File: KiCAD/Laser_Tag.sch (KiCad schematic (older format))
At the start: 20 parts, among them M1 MICROPHONE, P1 PHOTODETECTOR, Q1 2N3904, SW1 SW_PUSH, U1 PIC12LF

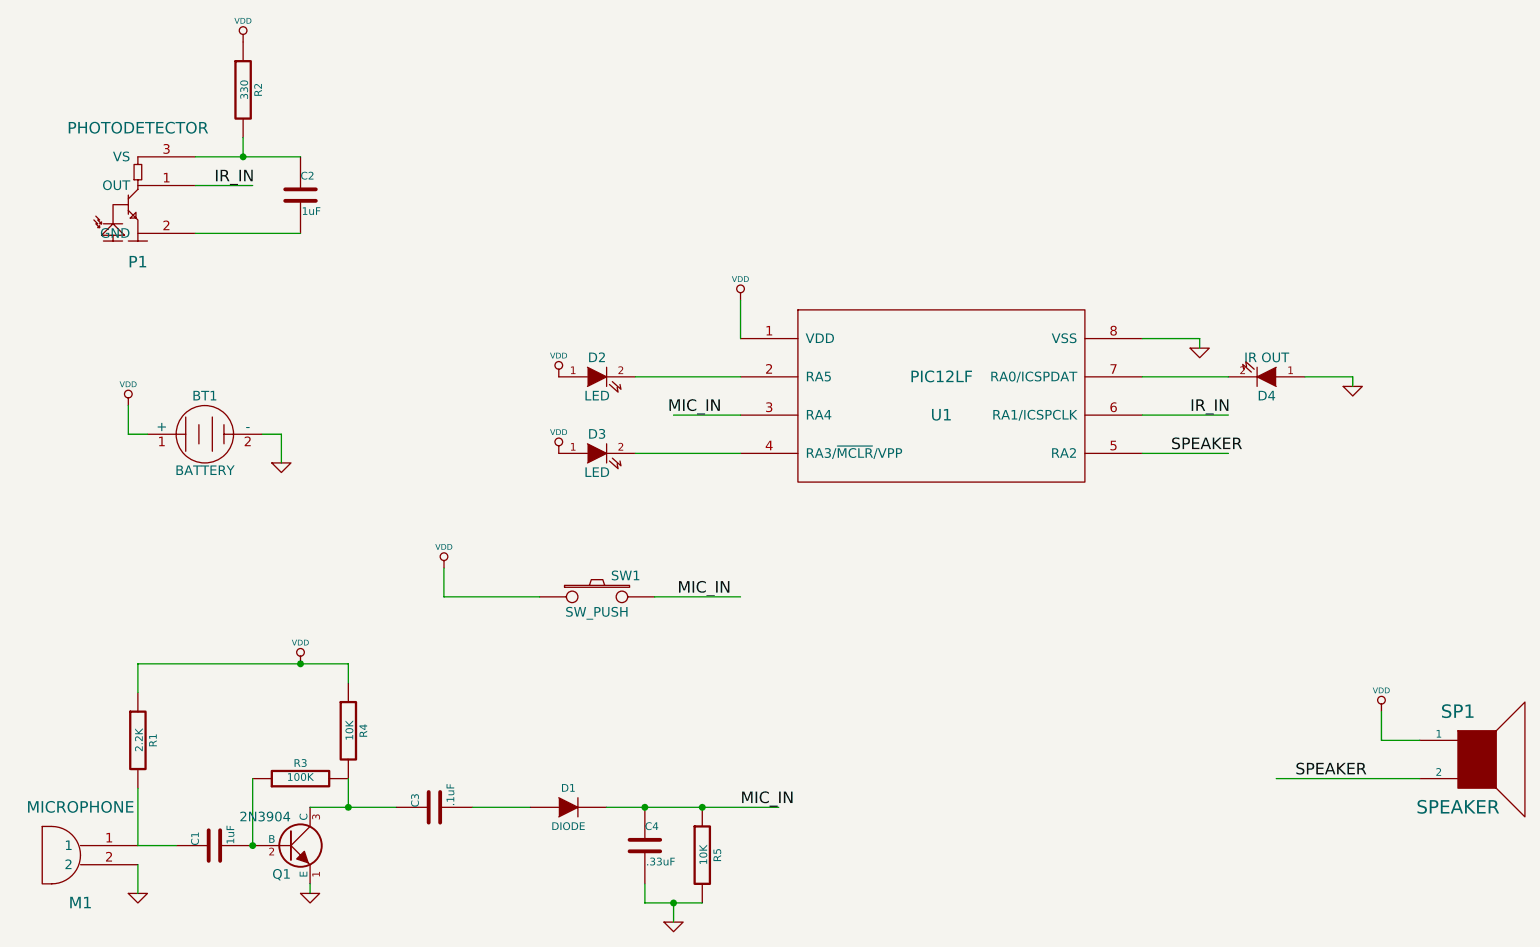
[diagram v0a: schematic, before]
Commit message: Changed component values, added video
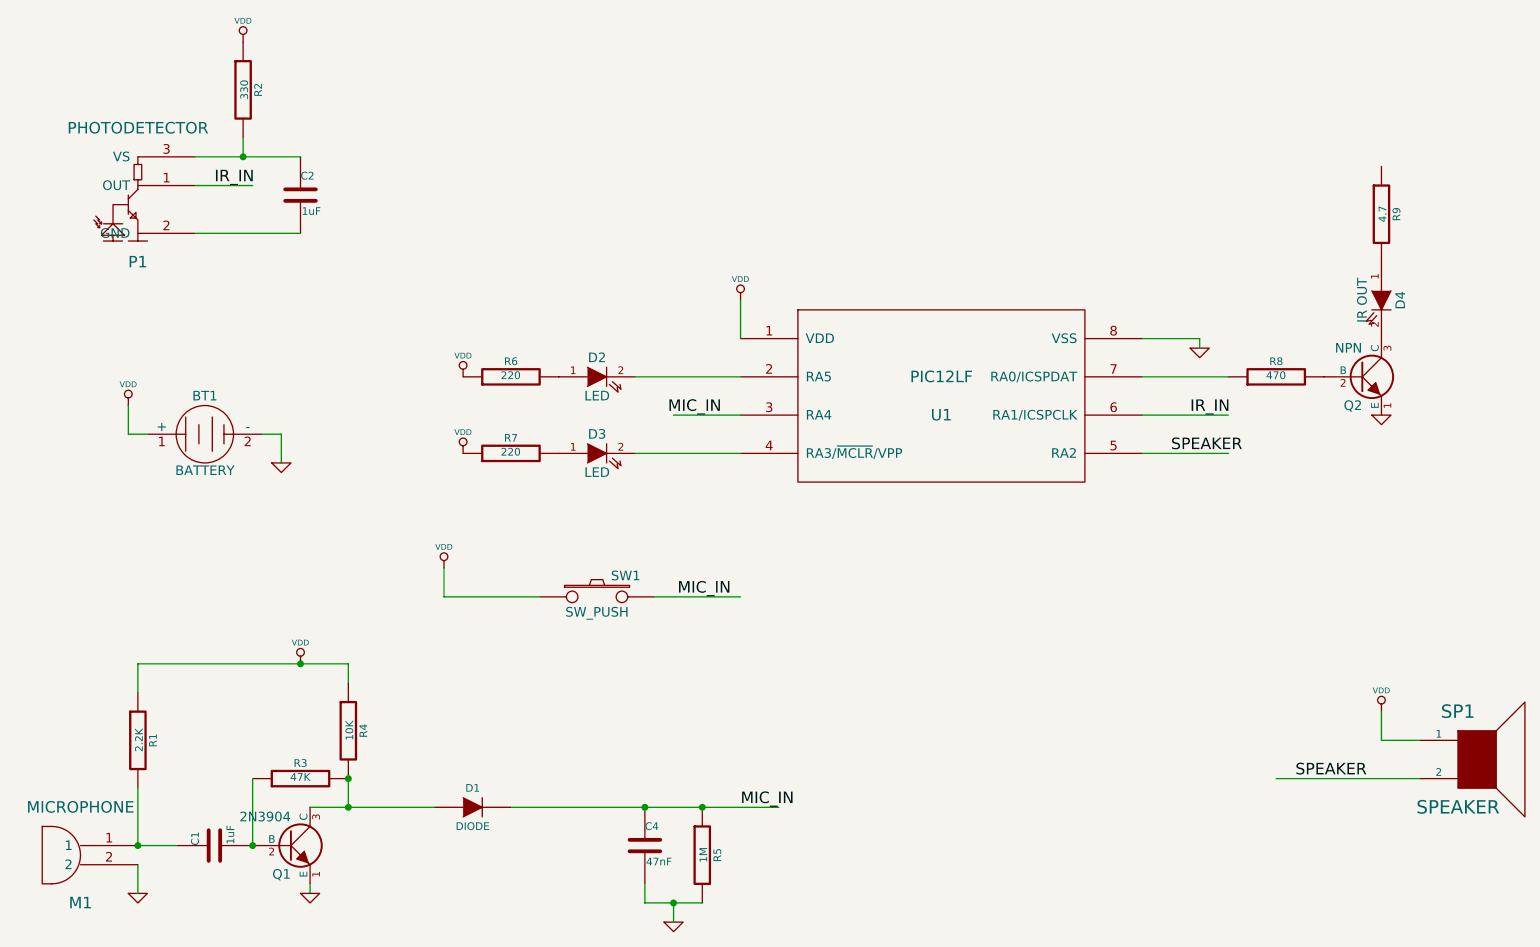
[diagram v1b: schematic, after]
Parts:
- removed C3: .1uF, ~, symbol C
- added Q2: NPN, ~, symbol NPN
- added R6, R7: 220, ~, symbol R
- added R8: 470, ~, symbol R
- added R9: 4.7, ~, symbol R
- C4: value .33uF -> 47nF
- R3: value 100K -> 47K
- R5: value 10K -> 1M
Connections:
- wire segments 40 -> 37
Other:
- moved on the sheet: D1, D4
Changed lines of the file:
@@
 Sheet 1 1
 Title ""
-Date "27 jul 2014"
+Date "28 jul 2014"
 Rev ""
 Comp ""
@@
 P 3850 5600
 F 0 "R3" V 3930 5600 40  0000 C CNN
-F 1 "100K" V 3857 5601 40  0000 C CNN
+F 1 "47K" V 3857 5601 40  0000 C CNN
 F 2 "~" V 3780 5600 30  0000 C CNN
 F 3 "~" H 3850 5600 30  0000 C CNN
@@
 	1    0    0    -1
 $EndComp
-$Comp
-L C C3
-U 1 1 53D53243
-P 4550 5750
-F 0 "C3" H 4550 5850 40  0000 L CNN
-F 1 ".1uF" H 4556 5665 40  0000 L CNN
-F 2 "~" H 4588 5600 30  0000 C CNN
-F 3 "~" H 4550 5750 60  0000 C CNN
-	1    4550 5750
-	0    -1   -1   0
-$EndComp
 Text Label 6150 5750 0    60   ~ 0
 MIC_IN
@@
 L LED D4
 U 1 1 53D53960
-P 8900 3500
-F 0 "D4" H 8900 3600 50  0000 C CNN
-F 1 "IR OUT" H 8900 3400 50  0000 C CNN
-F 2 "~" H 8900 3500 60  0000 C CNN
-F 3 "~" H 8900 3500 60  0000 C CNN
-	1    8900 3500
-	-1   0    0    1
+P 9500 3100
+F 0 "D4" H 9500 3200 50  0000 C CNN
+F 1 "IR OUT" H 9500 3000 50  0000 C CNN
+F 2 "~" H 9500 3100 60  0000 C CNN
+F 3 "~" H 9500 3100 60  0000 C CNN
+	1    9500 3100
+	0    1    1    0
 $EndComp
 Text Label 9050 5600 0    60   ~ 0
 SPEAKER
-Wire Wire Line
-	6150 3100 6150 3300
-Wire Wire Line
-	8250 3300 8550 3300
-Wire Wire Line
-	8550 3300 8550 3350
-Wire Wire Line
-	8950 5600 9700 5600
-Wire Wire Line
-	6150 3700 5800 3700
-Wire Wire Line
-	3000 5650 3000 5950
-Wire Wire Line
-	3000 6050 3000 6200
-Wire Wire Line
-	3000 5950 3200 5950
-Wire Wire Line
-	3900 6150 3900 6200
-Wire Wire Line
-	3000 5000 4100 5000
-Wire Wire Line
-	4100 5000 4100 5100
-Wire Wire Line
-	3000 5150 3000 5000
-Connection ~ 3850 5000
-Wire Wire Line
-	3600 5600 3600 5950
-Wire Wire Line
-	3900 5750 4350 5750
-Wire Wire Line
-	4100 5750 4100 5600
-Connection ~ 3600 5950
-Connection ~ 4100 5750
-Wire Wire Line
-	4750 5750 5050 5750
-Wire Wire Line
-	3300 2350 3850 2350
-Wire Wire Line
-	3550 2350 3550 2250
-Connection ~ 3550 2350
-Wire Wire Line
-	3300 2750 3850 2750
-Wire Wire Line
-	3300 2500 3600 2500
-Wire Wire Line
-	8250 3500 8700 3500
-Wire Wire Line
-	8250 3700 8700 3700
 Text Label 8500 3700 0    60   ~ 0
 IR_IN
-Wire Wire Line
-	8250 3900 8700 3900
 Text Label 8400 3900 0    60   ~ 0
 SPEAKER
@@
 	1    0    0    -1
 $EndComp
-Wire Wire Line
-	9500 5250 9500 5400
-Wire Wire Line
-	9500 5400 9700 5400
 $Comp
 L LED D2
@@
 L VDD #PWR8
 U 1 1 53D53E42
-P 5200 3500
-F 0 "#PWR8" H 5200 3600 30  0001 C CNN
-F 1 "VDD" H 5200 3610 30  0000 C CNN
-F 2 "" H 5200 3500 60  0000 C CNN
-F 3 "" H 5200 3500 60  0000 C CNN
-	1    5200 3500
+P 4700 3500
+F 0 "#PWR8" H 4700 3600 30  0001 C CNN
+F 1 "VDD" H 4700 3610 30  0000 C CNN
+F 2 "" H 4700 3500 60  0000 C CNN
+F 3 "" H 4700 3500 60  0000 C CNN
+	1    4700 3500
 	1    0    0    -1
 $EndComp
@@
 L VDD #PWR9
 U 1 1 53D53E51
-P 5200 3900
-F 0 "#PWR9" H 5200 4000 30  0001 C CNN
-F 1 "VDD" H 5200 4010 30  0000 C CNN
-F 2 "" H 5200 3900 60  0000 C CNN
-F 3 "" H 5200 3900 60  0000 C CNN
-	1    5200 3900
-	1    0    0    -1
-$EndComp
-Wire Wire Line
-	5600 3500 6150 3500
-Wire Wire Line
-	5600 3900 6150 3900
+P 4700 3900
+F 0 "#PWR9" H 4700 4000 30  0001 C CNN
+F 1 "VDD" H 4700 4010 30  0000 C CNN
+F 2 "" H 4700 3900 60  0000 C CNN
+F 3 "" H 4700 3900 60  0000 C CNN
+	1    4700 3900
+	1    0    0    -1
+$EndComp
 $Comp
 L BATTERY BT1
@@
 	1    0    0    -1
 $EndComp
-Wire Wire Line
-	3650 3800 3750 3800
-Wire Wire Line
-	3750 3800 3750 3950
 $Comp
 L VDD #PWR1
@@
 	1    0    0    -1
 $EndComp
-Wire Wire Line
-	3050 3800 2950 3800
-Wire Wire Line
-	2950 3800 2950 3650
 $Comp
 L SW_PUSH SW1
@@
 	1    0    0    -1
 $EndComp
-Wire Wire Line
-	5100 4650 4600 4650
-Wire Wire Line
-	5700 4650 6150 4650
 Text Label 6100 4650 2    60   ~ 0
 MIC_IN
@@
 	1    0    0    -1
 $EndComp
-Wire Wire Line
-	4600 4650 4600 4500
 $Comp
 L DIODE D1
 U 1 1 53D54A1B
-P 5250 5750
-F 0 "D1" H 5250 5850 40  0000 C CNN
-F 1 "DIODE" H 5250 5650 40  0000 C CNN
-F 2 "~" H 5250 5750 60  0000 C CNN
-F 3 "~" H 5250 5750 60  0000 C CNN
-	1    5250 5750
+P 4750 5750
+F 0 "D1" H 4750 5850 40  0000 C CNN
+F 1 "DIODE" H 4750 5650 40  0000 C CNN
+F 2 "~" H 4750 5750 60  0000 C CNN
+F 3 "~" H 4750 5750 60  0000 C CNN
+	1    4750 5750
 	1    0    0    -1
 $EndComp
@@
 P 5650 5950
 F 0 "C4" H 5650 6050 40  0000 L CNN
-F 1 ".33uF" H 5656 5865 40  0000 L CNN
+F 1 "47nF" H 5656 5865 40  0000 L CNN
 F 2 "~" H 5688 5800 30  0000 C CNN
 F 3 "~" H 5650 5950 60  0000 C CNN
@@
 P 5950 6000
 F 0 "R5" V 6030 6000 40  0000 C CNN
-F 1 "10K" V 5957 6001 40  0000 C CNN
+F 1 "1M" V 5957 6001 40  0000 C CNN
 F 2 "~" V 5880 6000 30  0000 C CNN
 F 3 "~" H 5950 6000 30  0000 C CNN
@@
 	1    0    0    -1
 $EndComp
-Wire Wire Line
-	5450 5750 6350 5750
-Connection ~ 5650 5750
-Wire Wire Line
-	5650 6150 5650 6250
-Wire Wire Line
-	5650 6250 5950 6250
 $Comp
 L GND #PWR10
@@
 	1    0    0    -1
 $EndComp
+$Comp
+L NPN Q2
+U 1 1 53D59463
+P 9400 3500
+F 0 "Q2" H 9400 3350 50  0000 R CNN
+F 1 "NPN" H 9400 3650 50  0000 R CNN
+F 2 "~" H 9400 3500 60  0000 C CNN
+F 3 "~" H 9400 3500 60  0000 C CNN
+	1    9400 3500
+	1    0    0    -1
+$EndComp
+$Comp
+L GND #PWR13
+U 1 1 53D5948E
+P 9500 3700
+F 0 "#PWR13" H 9500 3700 30  0001 C CNN
+F 1 "GND" H 9500 3630 30  0001 C CNN
+F 2 "" H 9500 3700 60  0000 C CNN
+F 3 "" H 9500 3700 60  0000 C CNN
+	1    9500 3700
+	1    0    0    -1
+$EndComp
+$Comp
+L R R9
+U 1 1 53D59496
+P 9500 2650
+F 0 "R9" V 9580 2650 40  0000 C CNN
+F 1 "4.7" V 9507 2651 40  0000 C CNN
+F 2 "~" V 9430 2650 30  0000 C CNN
+F 3 "~" H 9500 2650 30  0000 C CNN
+	1    9500 2650
+	1    0    0    -1
+$EndComp
+$Comp
+L R R8
+U 1 1 53D594A5
+P 8950 3500
+F 0 "R8" V 9030 3500 40  0000 C CNN
+F 1 "470" V 8957 3501 40  0000 C CNN
+F 2 "~" V 8880 3500 30  0000 C CNN
+F 3 "~" H 8950 3500 30  0000 C CNN
+	1    8950 3500
+	0    -1   -1   0
+$EndComp
+$Comp
+L R R6
+U 1 1 53D596C1
+P 4950 3500
+F 0 "R6" V 5030 3500 40  0000 C CNN
+F 1 "220" V 4957 3501 40  0000 C CNN
+F 2 "~" V 4880 3500 30  0000 C CNN
+F 3 "~" H 4950 3500 30  0000 C CNN
+	1    4950 3500
+	0    -1   -1   0
+$EndComp
+$Comp
+L R R7
+U 1 1 53D596DA
+P 4950 3900
+F 0 "R7" V 5030 3900 40  0000 C CNN
+F 1 "220" V 4957 3901 40  0000 C CNN
+F 2 "~" V 4880 3900 30  0000 C CNN
+F 3 "~" H 4950 3900 30  0000 C CNN
+	1    4950 3900
+	0    -1   -1   0
+$EndComp
+Wire Wire Line
+	6150 3100 6150 3300
+Wire Wire Line
+	8250 3300 8550 3300
+Wire Wire Line
+	8550 3300 8550 3350
+Wire Wire Line
+	8950 5600 9700 5600
+Wire Wire Line
+	6150 3700 5800 3700
+Wire Wire Line
+	3000 5650 3000 5950
+Wire Wire Line
+	3000 6050 3000 6200
+Wire Wire Line
+	3000 5950 3200 5950
+Wire Wire Line
+	3900 6150 3900 6200
+Wire Wire Line
+	3000 5000 4100 5000
+Wire Wire Line
+	4100 5000 4100 5100
+Wire Wire Line
+	3000 5150 3000 5000
+Connection ~ 3850 5000
+Wire Wire Line
+	3600 5600 3600 5950
+Wire Wire Line
+	4100 5750 4100 5600
+Connection ~ 3600 5950
+Connection ~ 4100 5750
+Wire Wire Line
+	3300 2350 3850 2350
+Wire Wire Line
+	3550 2350 3550 2250
+Connection ~ 3550 2350
+Wire Wire Line
+	3300 2750 3850 2750
+Wire Wire Line
+	3300 2500 3600 2500
+Wire Wire Line
+	8250 3500 8700 3500
+Wire Wire Line
+	8250 3700 8700 3700
+Wire Wire Line
+	8250 3900 8700 3900
+Wire Wire Line
+	9500 5250 9500 5400
+Wire Wire Line
+	9500 5400 9700 5400
+Wire Wire Line
+	5600 3500 6150 3500
+Wire Wire Line
+	5600 3900 6150 3900
+Wire Wire Line
+	3650 3800 3750 3800
+Wire Wire Line
+	3750 3800 3750 3950
+Wire Wire Line
+	3050 3800 2950 3800
+Wire Wire Line
+	2950 3800 2950 3650
+Wire Wire Line
+	5100 4650 4600 4650
+Wire Wire Line
+	5700 4650 6150 4650
+Wire Wire Line
+	4600 4650 4600 4500
+Wire Wire Line
+	4950 5750 6350 5750
+Connection ~ 5650 5750
+Wire Wire Line
+	5650 6150 5650 6250
+Wire Wire Line
+	5650 6250 5950 6250
 Wire Wire Line
 	5800 6250 5800 6350
 Connection ~ 5800 6250
 Connection ~ 5950 5750
-Wire Wire Line
-	9100 3500 9350 3500
-$Comp
-L GND #PWR13
-U 1 1 53D53A84
-P 9350 3550
-F 0 "#PWR13" H 9350 3550 30  0001 C CNN
-F 1 "GND" H 9350 3480 30  0001 C CNN
-F 2 "" H 9350 3550 60  0000 C CNN
-F 3 "" H 9350 3550 60  0000 C CNN
-	1    9350 3550
-	1    0    0    -1
-$EndComp
-Wire Wire Line
-	9350 3500 9350 3550
+Connection ~ 4100 5600
+Wire Wire Line
+	3900 5750 4550 5750
+Connection ~ 3000 5950
 $EndSCHEMATC

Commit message: First prototype version sent to PCB fab
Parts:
- Q2: value NPN -> 2N3904
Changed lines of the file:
@@
 $EndComp
 $Comp
-L VDD #PWR11
+L VDD #PWR01
 U 1 1 53D52EF1
 P 6150 3100
-F 0 "#PWR11" H 6150 3200 30  0001 C CNN
+F 0 "#PWR01" H 6150 3200 30  0001 C CNN
 F 1 "VDD" H 6150 3210 30  0000 C CNN
 F 2 "" H 6150 3100 60  0000 C CNN
@@
 $EndComp
 $Comp
-L GND #PWR12
+L GND #PWR02
 U 1 1 53D52F03
 P 8550 3350
-F 0 "#PWR12" H 8550 3350 30  0001 C CNN
+F 0 "#PWR02" H 8550 3350 30  0001 C CNN
 F 1 "GND" H 8550 3280 30  0001 C CNN
 F 2 "" H 8550 3350 60  0000 C CNN
@@
 $EndComp
 $Comp
-L VDD #PWR5
+L VDD #PWR03
 U 1 1 53D52F73
 P 3850 5000
-F 0 "#PWR5" H 3850 5100 30  0001 C CNN
+F 0 "#PWR03" H 3850 5100 30  0001 C CNN
 F 1 "VDD" H 3850 5110 30  0000 C CNN
 F 2 "" H 3850 5000 60  0000 C CNN
@@
 $EndComp
 $Comp
-L GND #PWR2
+L GND #PWR04
 U 1 1 53D52F95
 P 3000 6200
-F 0 "#PWR2" H 3000 6200 30  0001 C CNN
+F 0 "#PWR04" H 3000 6200 30  0001 C CNN
 F 1 "GND" H 3000 6130 30  0001 C CNN
 F 2 "" H 3000 6200 60  0000 C CNN
@@
 $EndComp
 $Comp
-L GND #PWR6
+L GND #PWR05
 U 1 1 53D52FF7
 P 3900 6200
-F 0 "#PWR6" H 3900 6200 30  0001 C CNN
+F 0 "#PWR05" H 3900 6200 30  0001 C CNN
 F 1 "GND" H 3900 6130 30  0001 C CNN
 F 2 "" H 3900 6200 60  0000 C CNN
@@
 $EndComp
 $Comp
-L VDD #PWR3
+L VDD #PWR06
 U 1 1 53D5377A
 P 3550 1750
-F 0 "#PWR3" H 3550 1850 30  0001 C CNN
+F 0 "#PWR06" H 3550 1850 30  0001 C CNN
 F 1 "VDD" H 3550 1860 30  0000 C CNN
 F 2 "" H 3550 1750 60  0000 C CNN
@@
 SPEAKER
 $Comp
-L VDD #PWR14
+L VDD #PWR07
 U 1 1 53D53BD1
 P 9500 5250
-F 0 "#PWR14" H 9500 5350 30  0001 C CNN
+F 0 "#PWR07" H 9500 5350 30  0001 C CNN
 F 1 "VDD" H 9500 5360 30  0000 C CNN
 F 2 "" H 9500 5250 60  0000 C CNN
@@
 $EndComp
 $Comp
-L VDD #PWR8
+L VDD #PWR08
 U 1 1 53D53E42
 P 4700 3500
-F 0 "#PWR8" H 4700 3600 30  0001 C CNN
+F 0 "#PWR08" H 4700 3600 30  0001 C CNN
 F 1 "VDD" H 4700 3610 30  0000 C CNN
 F 2 "" H 4700 3500 60  0000 C CNN
@@
 $EndComp
 $Comp
-L VDD #PWR9
+L VDD #PWR09
 U 1 1 53D53E51
 P 4700 3900
-F 0 "#PWR9" H 4700 4000 30  0001 C CNN
+F 0 "#PWR09" H 4700 4000 30  0001 C CNN
 F 1 "VDD" H 4700 4010 30  0000 C CNN
 F 2 "" H 4700 3900 60  0000 C CNN
@@
 $EndComp
 $Comp
-L GND #PWR4
+L GND #PWR010
 U 1 1 53D5401E
 P 3750 3950
-F 0 "#PWR4" H 3750 3950 30  0001 C CNN
+F 0 "#PWR010" H 3750 3950 30  0001 C CNN
 F 1 "GND" H 3750 3880 30  0001 C CNN
 F 2 "" H 3750 3950 60  0000 C CNN
@@
 $EndComp
 $Comp
-L VDD #PWR1
+L VDD #PWR011
 U 1 1 53D5404F
 P 2950 3650
-F 0 "#PWR1" H 2950 3750 30  0001 C CNN
+F 0 "#PWR011" H 2950 3750 30  0001 C CNN
 F 1 "VDD" H 2950 3760 30  0000 C CNN
 F 2 "" H 2950 3650 60  0000 C CNN
@@
 MIC_IN
 $Comp
-L VDD #PWR7
+L VDD #PWR012
 U 1 1 53D5492C
 P 4600 4500
-F 0 "#PWR7" H 4600 4600 30  0001 C CNN
+F 0 "#PWR012" H 4600 4600 30  0001 C CNN
 F 1 "VDD" H 4600 4610 30  0000 C CNN
 F 2 "" H 4600 4500 60  0000 C CNN
@@
 $EndComp
 $Comp
-L GND #PWR10
+L GND #PWR013
 U 1 1 53D54AC4
 P 5800 6350
-F 0 "#PWR10" H 5800 6350 30  0001 C CNN
+F 0 "#PWR013" H 5800 6350 30  0001 C CNN
 F 1 "GND" H 5800 6280 30  0001 C CNN
 F 2 "" H 5800 6350 60  0000 C CNN
@@
 P 9400 3500
 F 0 "Q2" H 9400 3350 50  0000 R CNN
-F 1 "NPN" H 9400 3650 50  0000 R CNN
+F 1 "2N3904" H 9400 3650 50  0000 R CNN
 F 2 "~" H 9400 3500 60  0000 C CNN
 F 3 "~" H 9400 3500 60  0000 C CNN
@@
 $EndComp
 $Comp
-L GND #PWR13
+L GND #PWR014
 U 1 1 53D5948E
 P 9500 3700
-F 0 "#PWR13" H 9500 3700 30  0001 C CNN
+F 0 "#PWR014" H 9500 3700 30  0001 C CNN
 F 1 "GND" H 9500 3630 30  0001 C CNN
 F 2 "" H 9500 3700 60  0000 C CNN
@@
 	3900 5750 4550 5750
 Connection ~ 3000 5950
+$Comp
+L VDD #PWR015
+U 1 1 53D5BD92
+P 9500 2400
+F 0 "#PWR015" H 9500 2500 30  0001 C CNN
+F 1 "VDD" H 9500 2510 30  0000 C CNN
+F 2 "" H 9500 2400 60  0000 C CNN
+F 3 "" H 9500 2400 60  0000 C CNN
+	1    9500 2400
+	1    0    0    -1
+$EndComp
 $EndSCHEMATC
